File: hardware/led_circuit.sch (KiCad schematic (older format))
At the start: 3 parts

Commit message: layout first draft
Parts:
- R34, R35: renamed from R?; footprint (none) -> Resistor_SMD:R_0805_2012Metric_Pad1.15x1.40mm_HandSolder
- gave numbers to parts that had none: 1
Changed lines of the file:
@@
 $Descr A4 11693 8268
 encoding utf-8
-Sheet 9 10
+Sheet 8 10
 Title ""
 Date ""
@@
 AR Path="/5C0C9B56/5C0CCB6F" Ref="Q?"  Part="1"
 AR Path="/5C0C9BDB/5C0CCB6F" Ref="Q?"  Part="1"
-AR Path="/5C0CCA50/5C0CCB6F" Ref="Q?"  Part="1"
-AR Path="/5C0CD9EF/5C0CCB6F" Ref="Q?"  Part="1"
-AR Path="/5C0CDD32/5C0CCB6F" Ref="Q?"  Part="1"
+AR Path="/5C0CCA50/5C0CCB6F" Ref="Q11"  Part="1"
+AR Path="/5C0CD9EF/5C0CCB6F" Ref="Q12"  Part="1"
+AR Path="/5C0CDD32/5C0CCB6F" Ref="Q13"  Part="1"
 AR Path="/5C0D9062/5C0CCB6F" Ref="Q?"  Part="1"
-F 0 "Q?" V 3850 3650 50  0000 L CNN
+F 0 "Q11" V 3850 3650 50  0000 L CNN
 F 1 "2N7002" V 3850 3250 50  0000 L CNN
 F 2 "Package_TO_SOT_SMD:SOT-23" H 3800 3525 50  0001 L CIN
@@
 AR Path="/5C0C9B56/5C0CCB76" Ref="#PWR?"  Part="1"
 AR Path="/5C0C9BDB/5C0CCB76" Ref="#PWR?"  Part="1"
-AR Path="/5C0CCA50/5C0CCB76" Ref="#PWR?"  Part="1"
-AR Path="/5C0CD9EF/5C0CCB76" Ref="#PWR?"  Part="1"
-AR Path="/5C0CDD32/5C0CCB76" Ref="#PWR?"  Part="1"
+AR Path="/5C0CCA50/5C0CCB76" Ref="#PWR090"  Part="1"
+AR Path="/5C0CD9EF/5C0CCB76" Ref="#PWR091"  Part="1"
+AR Path="/5C0CDD32/5C0CCB76" Ref="#PWR092"  Part="1"
 AR Path="/5C0D9062/5C0CCB76" Ref="#PWR?"  Part="1"
-F 0 "#PWR?" H 3700 3550 50  0001 C CNN
+F 0 "#PWR092" H 3700 3550 50  0001 C CNN
 F 1 "GND" H 3700 3650 50  0000 C CNN
 F 2 "" H 3700 3800 50  0000 C CNN
@@
 AR Path="/5C0C9B56/5C0CCB7C" Ref="R?"  Part="1"
 AR Path="/5C0C9BDB/5C0CCB7C" Ref="R?"  Part="1"
-AR Path="/5C0CCA50/5C0CCB7C" Ref="R?"  Part="1"
-AR Path="/5C0CD9EF/5C0CCB7C" Ref="R?"  Part="1"
-AR Path="/5C0CDD32/5C0CCB7C" Ref="R?"  Part="1"
+AR Path="/5C0CCA50/5C0CCB7C" Ref="R34"  Part="1"
+AR Path="/5C0CD9EF/5C0CCB7C" Ref="R36"  Part="1"
+AR Path="/5C0CDD32/5C0CCB7C" Ref="R38"  Part="1"
 AR Path="/5C0D9062/5C0CCB7C" Ref="R?"  Part="1"
-F 0 "R?" V 3043 3600 50  0000 C CNN
+F 0 "R34" V 3043 3600 50  0000 C CNN
 F 1 "100R" V 3134 3600 50  0000 C CNN
-F 2 "" V 3180 3600 50  0001 C CNN
+F 2 "Resistor_SMD:R_0805_2012Metric_Pad1.15x1.40mm_HandSolder" V 3180 3600 50  0001 C CNN
 F 3 "~" H 3250 3600 50  0001 C CNN
 	1    3250 3600
@@
 AR Path="/5C0C9B56/5C0CCBAB" Ref="R?"  Part="1"
 AR Path="/5C0C9BDB/5C0CCBAB" Ref="R?"  Part="1"
-AR Path="/5C0CCA50/5C0CCBAB" Ref="R?"  Part="1"
-AR Path="/5C0CD9EF/5C0CCBAB" Ref="R?"  Part="1"
-AR Path="/5C0CDD32/5C0CCBAB" Ref="R?"  Part="1"
+AR Path="/5C0CCA50/5C0CCBAB" Ref="R35"  Part="1"
+AR Path="/5C0CD9EF/5C0CCBAB" Ref="R37"  Part="1"
+AR Path="/5C0CDD32/5C0CCBAB" Ref="R39"  Part="1"
 AR Path="/5C0D9062/5C0CCBAB" Ref="R?"  Part="1"
-F 0 "R?" H 3630 3204 50  0000 R CNN
+F 0 "R35" H 3630 3204 50  0000 R CNN
 F 1 "2k2" H 3630 3295 50  0000 R CNN
-F 2 "" V 3630 3250 50  0001 C CNN
+F 2 "Resistor_SMD:R_0805_2012Metric_Pad1.15x1.40mm_HandSolder" V 3630 3250 50  0001 C CNN
 F 3 "~" H 3700 3250 50  0001 C CNN
 	1    3700 3250

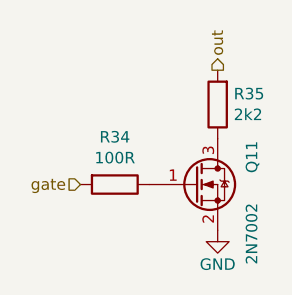
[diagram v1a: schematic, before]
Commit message: added testpoints and silkscreen
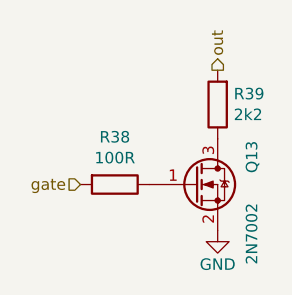
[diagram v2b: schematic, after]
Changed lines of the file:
@@
 AR Path="/5C0CDD32/5C0CCB6F" Ref="Q13"  Part="1"
 AR Path="/5C0D9062/5C0CCB6F" Ref="Q?"  Part="1"
-F 0 "Q11" V 3850 3650 50  0000 L CNN
+F 0 "Q13" V 3850 3650 50  0000 L CNN
 F 1 "2N7002" V 3850 3250 50  0000 L CNN
 F 2 "Package_TO_SOT_SMD:SOT-23" H 3800 3525 50  0001 L CIN
@@
 AR Path="/5C0CDD32/5C0CCB7C" Ref="R38"  Part="1"
 AR Path="/5C0D9062/5C0CCB7C" Ref="R?"  Part="1"
-F 0 "R34" V 3043 3600 50  0000 C CNN
+F 0 "R38" V 3043 3600 50  0000 C CNN
 F 1 "100R" V 3134 3600 50  0000 C CNN
 F 2 "Resistor_SMD:R_0805_2012Metric_Pad1.15x1.40mm_HandSolder" V 3180 3600 50  0001 C CNN
@@
 AR Path="/5C0CDD32/5C0CCBAB" Ref="R39"  Part="1"
 AR Path="/5C0D9062/5C0CCBAB" Ref="R?"  Part="1"
-F 0 "R35" H 3630 3204 50  0000 R CNN
+F 0 "R39" H 3630 3204 50  0000 R CNN
 F 1 "2k2" H 3630 3295 50  0000 R CNN
 F 2 "Resistor_SMD:R_0805_2012Metric_Pad1.15x1.40mm_HandSolder" V 3630 3250 50  0001 C CNN
